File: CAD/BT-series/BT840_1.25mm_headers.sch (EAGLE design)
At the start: 62 parts, among them J1 SM02B-SRSS-TB(LF)(SN), U1 LP5907MFX-3.3/NOPB, U2 DX4R005JJ2R1800, U3 LP5907MFX-3.3/NOPB, U4 ADS131M08IPBS, U5 BQ24072RGTR, U6 TPD4S012DRYR, X1 ABM3B-8.000MHZ-B2-T, X5 1365-16

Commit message: added revisions and alt configurations
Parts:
- removed HDR1, HDR2: 1365-20, con-leotronics:1365-20
- removed MCU: BC40M, BC40M-V0-lib2:BC40M
- removed R22: 348kΩ, standardparts:RESISTOR.0201
- removed R23: 750kΩ, standardparts:RESISTOR.0201
- removed R24: 100kΩ, standardparts:RESISTOR.0201
- removed R25: 0Ω, standardparts:RESISTOR.0805
- removed R26: 3.3kΩ, standardparts:RESISTOR.0201
- removed R27: 10kΩ, standardparts:RESISTOR.0201
- removed R28, R29: 10kΩ, standardparts:RESISTOR.0402
- removed R30, R31: 100kΩ, standardparts:RESISTOR.0402
- added C30: 0.1uF, standardparts:CAPACITOR.0201
- added C31: 10uF, standardparts:CAPACITOR.0402
- added LED3: (no value), adafruit:LEDCHIPLED_0603
- added R10, R11: 10kΩ, standardparts:RESISTOR.0402
- added R12, R13: 100kΩ, standardparts:RESISTOR.0402
- added R6: 348kΩ, standardparts:RESISTOR.0201
- added R7: 750kΩ, standardparts:RESISTOR.0201
- added R8, R9: 3.3kΩ, standardparts:RESISTOR.0201
- added U7: DX4R005JJ2R1800, DX4R005JJ2R1800:DX4R005JJ2R1800
- added X2: FC-12M, crystal:FC-12M
- added X3, X4: 1365-20, con-leotronics:1365-20
- C1, C2: value 10pF -> 12.5pF
- C12: value 4.7uF -> 1uF
- C13: value 100pF -> 1uF
- C14: value 100pF -> 4.7uF
- C15: value 100pF -> 10uF; device standardparts:CAPACITOR.0201 -> standardparts:CAPACITOR.0402
- C18: value 100pF -> 0.1uF
- C19: value 100pF -> 10nF
- C21, C28: value 0.1uF -> 100pF
- C22: value 10nF -> 0.1uF
- C23: value 0.1uF -> 1uF
- C24: value 1uF -> 100pF
- C25: value 4.7uF -> 100pF
- C29: value 10uF -> 100pF; device standardparts:CAPACITOR.0402 -> standardparts:CAPACITOR.0201
- C3: value 1uF -> 10pF
- C4: value 220nF -> 10pF
- C6: value 1uF -> 220nF
- C9: value 10uF -> 4.7uF; device standardparts:CAPACITOR.0402 -> standardparts:CAPACITOR.0201
- LED1: value GM5WA94310A -> (none); device led:GM5WA94310A -> adafruit:LEDCHIPLED_0603
- R1: value 3.3kΩ -> 10kΩ
- R2: value 3.3kΩ -> 100kΩ
- R3: value 3.3kΩ -> 1.18kΩ; SPICEPREFIX (none) -> R
- R4: value 1.18kΩ -> 1.13kΩ; SPICEPREFIX R -> (none)
- R5: value 1.13kΩ -> 3.3kΩ
- U1: value LP5907MFX-3.3/NOPB -> TPD4S012DRYR; device LP5907MFX-3.3_NOPB:LP5907MFX-3.3/NOPB -> TPD4S012DRYR:TPD4S012DRYR
- U2: value DX4R005JJ2R1800 -> BT840; device DX4R005JJ2R1800:DX4R005JJ2R1800 -> BT840:BT840
- U4: value ADS131M08IPBS -> LP5907MFX-3.3/NOPB; device ADS131M08IPBS:ADS131M08IPBS -> LP5907MFX-3.3_NOPB:LP5907MFX-3.3/NOPB
- U5: value BQ24072RGTR -> ADS131M08IPBS; device BQ24072RGTR:BQ24072RGTR -> ADS131M08IPBS:ADS131M08IPBS
- U6: value TPD4S012DRYR -> BQ24072RGTR; device TPD4S012DRYR:TPD4S012DRYR -> BQ24072RGTR:BQ24072RGTR
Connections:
- removed net LED5: LED2.A, R26.2
- removed net N$1: LED1R.A, R3.2
- removed net N$2: LED1G.A, R2.2
- removed net N$3: LED1B.A, R1.2
- removed net P102: HDR1-16.S, MCU.C5/P102/I2C
- removed net P10_MISO: HDR2-1.S, MCU.G7/P010/MISO
- removed net P14: HDR1-13.S, MCU.B4/P014/QSPI1
- removed net P15: HDR1-8.S, MCU.A4/015/QSPI2
- removed net P16: HDR1-3.S, MCU.B5/P016/QSPI3
- removed net P18: HDR1-11.S, MCU.B3/P018/QSPI_CS
- removed net P19: MCU.C3/P019, R3.1
- removed net P25_AIN4: HDR2-6.S, MCU.B0/P025/AIN4
- removed net P26_AIN5: HDR1-1.S, MCU.C1/P026/AIN5
- removed net P27_AIN6: HDR2-8.S, MCU.C0/P027/AIN6
- removed net P28_AIN7: HDR2-4.S, MCU.F1/P028/AIN7
- removed net P29: MCU.E1/P029, R2.1
- removed net P30: HDR2-11.S, MCU.G1/P030
- removed net P4_AIN0: HDR1-17.S, MCU.D5/P004/AIN0
- removed net P5_AIN1: HDR1-15.S, MCU.D4/P005/AIN1
- removed net P6_AIN2: HDR1-19.S, MCU.D7/P006/AIN2
- removed net P7_AIN3: HDR1-20.S, MCU.B6/P007/AIN3
- removed net P9_MOSI: HDR2-2.S, MCU.C4/P9/MOSI
- removed net VDDH: MCU.F6/VDDH, R24.2, R25.1, R28.1, R29.1
- new net DCCH: U2.DCCH, X4-20.S
- new net LED1: LED1.A, R5.2
- new net LED2: LED2.A, R8.2
- new net LED3: LED3.A, R9.2
- new net P100: U2.P1.00, X4-13.S
- new net P107: U2.P1.07, X4-18.S
- new net P108: U2.P1.08, X3-9.S
- new net P11: U2.P0.11, X4-15.S
- new net P112: U2.P1.12, X4-4.S
- new net P25: R5.1, U2.P0.25
- new net P26_SDA: U2.P0.26/SDA, X3-8.S
- new net P27_SCL: U2.P0.27/SCL, X3-10.S
- new net P28_AIN4: U2.P0.28/AIN4, X4-6.S
- new net P29_AIN5: U2.P0.29/AIN5, X4-14.S
- new net P2_AIN0: U2.P0.02/AIN0, X3-16.S
- new net P30_AIN6: U2.P0.30/AIN6, X4-8.S
- new net P31_AIN7: U2.P0.31/AIN7, X3-1.S
- new net P3_AIN1: U2.P0.03/AIN1, X3-18.S
- new net P4_AIN2: U2.P0.04/AIN2, X3-4.S
- new net P5_AIN3: U2.P0.05/AIN3, X3-20.S
- new net P7: U2.P0.07, X3-5.S
- new net XTAL1_1: C2.2, U2.P0.00/XL1, X2.2
- new net XTAL2_1: C1.2, U2.P0.01/XL2, X2.1
- net +5V: now also C19.2, C30.2, C31.2, C9.2, U1.VBUS, U7.1; no longer C22.2, C25.2, C28.2, C29.2, U2.1, U6.VBUS
- net +5V_ISO: now also C18.1, U2.VBUS, U6.IN; no longer C21.1, MCU.F5/VBUS, U5.IN
- net 0N: now also C16.2, U5.AN0N; no longer C13.2, U4.AN0N
- net 0P: now also C16.1, U5.AN0P; no longer C13.1, U4.AN0P
- net 1N: now also C17.2, U5.AN1N; no longer C14.2, U4.AN1N
- net 1P: now also C17.1, U5.AN1P; no longer C14.1, U4.AN1P
- net 2N: now also C20.2, U5.AIN2N; no longer C15.2, U4.AIN2N
- net 2P: now also C20.1, U5.AIN2P; no longer C15.1, U4.AIN2P
- net 3N: now also C21.2, U5.AIN3N; no longer C16.2, U4.AIN3N
- net 3P: now also C21.1, U5.AIN3P; no longer C16.1, U4.AIN3P
- net 4N: now also C24.2, U5.AIN4N; no longer C17.2, U4.AIN4N
- net 4P: now also C24.1, U5.AIN4P; no longer C17.1, U4.AIN4P
- net 5N: now also C25.2, U5.AIN5N; no longer C18.2, U4.AIN5N
- net 5P: now also C25.1, U5.AIN5P; no longer C18.1, U4.AIN5P
- net 6N: now also C28.2, U5.AIN6N; no longer C19.2, U4.AIN6N
- net 6P: now also C28.1, U5.AIN6P; no longer C19.1, U4.AIN6P
- net 7N: now also C29.2, U5.AIN7N; no longer C20.2, U4.AIN7N
- net 7P: now also C29.1, U5.AIN7P; no longer C20.1, U4.AIN7P
- net AVDD: now also C5.2, C8.1, U4.OUT, U5.AVDD; no longer C3.2, C6.1, U3.OUT, U4.AVDD
- net BAT: now also C14.2, R6.1, U6.BAT@2, U6.BAT@3; no longer C12.2, R22.1, U5.BAT@2, U5.BAT@3
- net CAP: now also C6.1, U5.CAP; no longer C4.1, U4.CAP
- net CHG: now also R11.2, U2.P0.23, U6.!CHG; no longer MCU.C7/P008, R29.2, U5.!CHG
- net CLKIN: now also C3.1, U5.XTAL1; no longer C1.1, U4.XTAL1
- net CLKOUT: now also C4.1, U5.XTAL2; no longer C2.1, HDR2-20.S, U4.XTAL2
- net CS: now also R13.1, U2.P1.01, U5.CS; no longer MCU.E4/P101, R31.1, U4.CS
- net CUR_DETECT: now also R6.2, R7.1, U2.P0.16; no longer MCU.E7/P011, R22.2, R23.1
- net D+: now also U1.D+, U2.D+, U7.3; no longer MCU.H5/D+, U2.3, U6.D+
- net D-: now also U1.D-, U2.D-, U7.2; no longer MCU.G5/D-, U2.2, U6.D-
- net DIN: now also U2.P0.14, U5.DIN, X3-17.S; no longer HDR2-17.S, MCU.F2/P108, U4.DIN
- net DOUT: now also R12.1, U2.P1.02, U5.DOUT, X3-14.S; no longer HDR2-15.S, MCU.F3/P112, R30.1, U4.DOUT
- net DRDY: now also U2.P0.06, U5.DRDY; no longer MCU.E3/P031, U4.DRDY
- net GND: now also C1.1, C13.1, C14.1, C15.1, C18.2, C19.1, C2.1, C3.2, C30.1, C31.1, C5.1, C7.2, C8.2, LED1.C, LED3.C, R1.1, R12.2, R3.1, R7.2, U2.GND, U4.GND, U5.AGND, U5.AGND-1, U5.DGND, U6.!CE, U6.EN1, U6.TD, U6.VSS, U7.5, U7.MP1, U7.MP2, X4-17.S; no longer C1.2, C2.2, C21.2, C24.1, C25.1, C28.1, C29.1, C3.1, C5.2, C7.1, C8.1, HDR2-16.S, LED1B.C, LED1G.C, LED1R.C, MCU.D3/VSS, MCU.E0/GND, MCU.F0/GND, MCU.F4/GND, MCU.G0/VSS, MCU.H0/GND, MCU.H1/GND, MCU.H7/VSS, R23.2, R27.1, R5.1, U2.5, U2.MP1, U2.MP2, U4.AGND, U4.AGND-1, U4.DGND, U5.!CE, U5.EN1, U5.TD, U5.VSS, U6.GND
- net ID: now also U7.4; no longer U2.4
- net ILM: now also R3.2, U6.ILIM; no longer R4.2, U5.ILIM
- net ISET: now also R4.2, U6.ISET; no longer R5.2, U5.ISET
- net NFC1: now also U2.P0.09/NFC1; no longer MCU.F7/P002/NFC1
- net NFC2: now also U2.P0.10/NFC2; no longer MCU.C6/NFC2
- net P103: now also U2.P1.03, X3-11.S; no longer HDR1-5.S, MCU.E6/P103/I2C
- net P104: now also U2.P1.04, X3-15.S; no longer HDR1-2.S, MCU.A1/P104
- net P105: now also U2.P1.05, X3-19.S; no longer HDR1-12.S, MCU.A6/P105
- net P106: now also U2.P1.06, X3-7.S; no longer HDR1-14.S, MCU.A7/P106
- net P109: now also U2.P1.09, X4-1.S; no longer MCU.A0/P109, R26.1
- net P110: now also U2.P1.10, X3-3.S; no longer HDR2-9.S, MCU.G2/P110
- net P111: now also U2.P1.11, X4-2.S; no longer HDR2-3.S, MCU.H2/P111
- net P113: now also U2.P1.13, X3-2.S; no longer HDR2-5.S, MCU.G3/P113
- net P114: now also U2.P1.14, X3-6.S; no longer HDR2-7.S, MCU.H3/P114
- net P115: now also U2.P1.15, X3-12.S; no longer HDR2-19.S, MCU.H4/P115
- net P12: now also U2.P0.12, X4-3.S; no longer HDR1-18.S, MCU.B7/P012/SPI_DCX
- net P13: now also U2.P0.13, X4-11.S; no longer HDR1-10.S, MCU.A5/013/QSPI0
- net P17: now also U2.P0.17, X4-10.S; no longer HDR1-6.S, MCU.A3/P017/QSPI_CLK
- net P20: now also R9.1, U2.P0.20; no longer HDR1-4.S, MCU.A2/P020
- net P21: now also R8.1, U2.P0.21; no longer MCU.C2/P021, R1.1
- net P22: now also U2.P0.22, X4-12.S; no longer HDR1-9.S, MCU.B2/P022
- net P24: now also U2.P0.24, X4-16.S; no longer HDR1-7.S, MCU.B1/P024
- net PGOOD: now also R10.2, U2.P0.19, U6.!PGOOD; no longer MCU.D6/P023, R28.2, U5.!PGOOD
- net RESET: now also R2.1, U2.P0.18/RESET, X4-9.S; no longer HDR2-14.S, MCU.D2/RESET, R24.1
- net SCLK: now also U2.P0.15, U5.SCLK, X3-13.S; no longer HDR2-13.S, MCU.E2/P107, U4.SCLK
- net SWDCLK: now also U2.SWDCLK, X4-7.S; no longer HDR2-10.S, MCU.D1/SWDCLK
- net SWDIO: now also U2.SWDIO, X4-5.S; no longer HDR2-12.S, MCU.D0/SWDIO
- net SYNC/RESET: now also U2.P0.08, U5.SYNC/RESET; no longer MCU.E5/P100, U4.SYNC/RESET
- net TMR: now also U6.TMR; no longer U5.TMR
- net TS: now also R1.2, U6.TS; no longer R27.2, U5.TS
- net VDD: now also C12.2, C15.2, C22.2, R10.1, R11.1, R13.2, R2.2, U2.VDD, U2.VDDH, U3.OUT, U5.DVDD, X4-19.S; no longer C7.2, C9.2, HDR2-18.S, MCU.G4/VDD, R25.2, R30.2, U1.OUT, U4.DVDD
- net VIN: now also C13.2, C7.1, U4.EN, U4.IN; no longer C24.2, C5.1, C8.2, R31.2, U1.EN, U1.IN
- net VSWITCH: now also U6.EN2, U6.OUT@10, U6.OUT@11; no longer U5.EN2, U5.OUT@10, U5.OUT@11
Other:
- note added: "830050789"
- note added: "BC840M"
- note removed: "BC40M"
- note removed: "L1MC-RGB0028000MP0 (OR OTHER)"
- moved on the sheet: C1, C10, C11, C12, C13, C14, C15, C16, C17, C18, C19, C2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

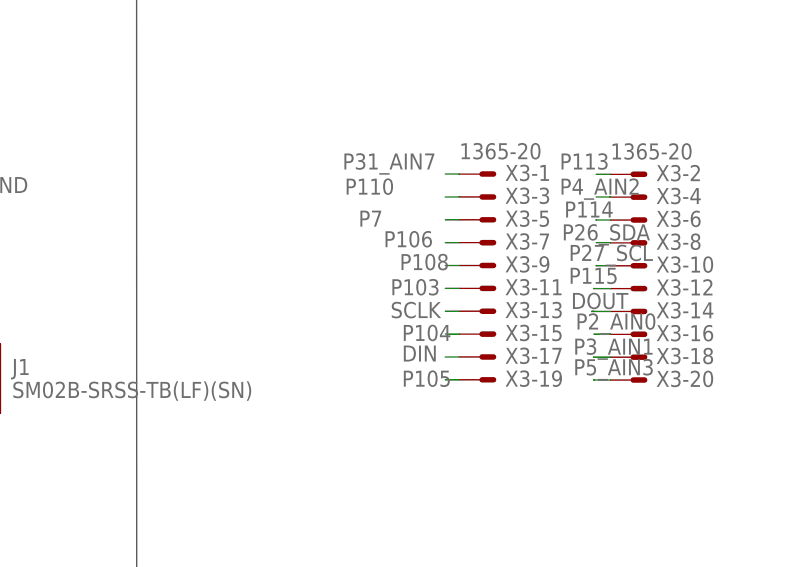
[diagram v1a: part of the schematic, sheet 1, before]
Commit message: fixed CLKOUT GPIO pin missing, replaced P105 breakout
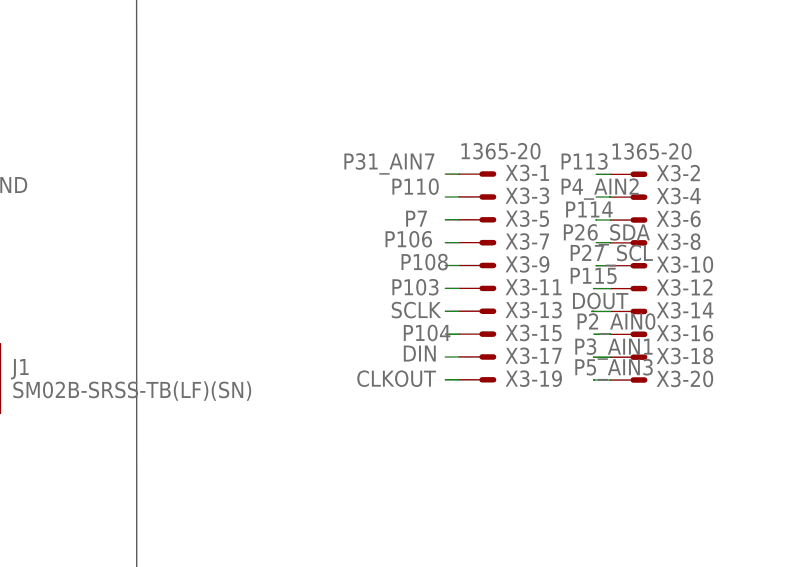
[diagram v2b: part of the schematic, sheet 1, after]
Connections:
- net CLKOUT: now also X3-19.S
- net P105: no longer X3-19.S
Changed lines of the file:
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@@
 <setting verticaltext="up"/>
 </settings>
-<grid distance="10" unitdist="mil" unit="mil" style="lines" multiple="1" display="no" altdistance="0.01" altunitdist="inch" altunit="inch"/>
+<grid distance="0.1" unitdist="inch" unit="inch" style="lines" multiple="1" display="no" altdistance="0.01" altunitdist="inch" altunit="inch"/>
 <layers>
 <layer number="1" name="Top" color="4" fill="1" visible="no" active="no"/>
@@
 <pinref part="X3" gate="-5" pin="S"/>
 <wire x1="192.0494" y1="53.594" x2="190.5" y2="53.594" width="0.1524" layer="91"/>
-<label x="180.848" y="52.832" size="1.778" layer="95"/>
+<label x="185.928" y="52.832" size="1.778" layer="95"/>
 </segment>
 </net>
@@
 <pinref part="X3" gate="-3" pin="S"/>
 <wire x1="192.0494" y1="56.134" x2="190.5" y2="56.134" width="0.1524" layer="91"/>
-<label x="179.324" y="56.388" size="1.778" layer="95"/>
+<label x="184.404" y="56.388" size="1.778" layer="95"/>
 </segment>
 </net>
@@
 <label x="507.365" y="139.3698" size="1.778" layer="95"/>
 </segment>
+<segment>
+<pinref part="X3" gate="-19" pin="S"/>
+<wire x1="192.0494" y1="35.814" x2="190.5" y2="35.814" width="0.1524" layer="91"/>
+<label x="180.594" y="35.052" size="1.778" layer="95"/>
+</segment>
 </net>
 <net name="TMR" class="0">
@@
 <label x="284.988" y="146.304" size="1.778" layer="95"/>
 </segment>
-<segment>
-<pinref part="X3" gate="-19" pin="S"/>
-<wire x1="192.0494" y1="35.814" x2="190.5" y2="35.814" width="0.1524" layer="91"/>
-<label x="185.674" y="35.052" size="1.778" layer="95"/>
-</segment>
-</net>
+</net>
